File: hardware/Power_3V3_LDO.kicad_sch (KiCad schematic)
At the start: 5 parts, among them U1 MCP1826S

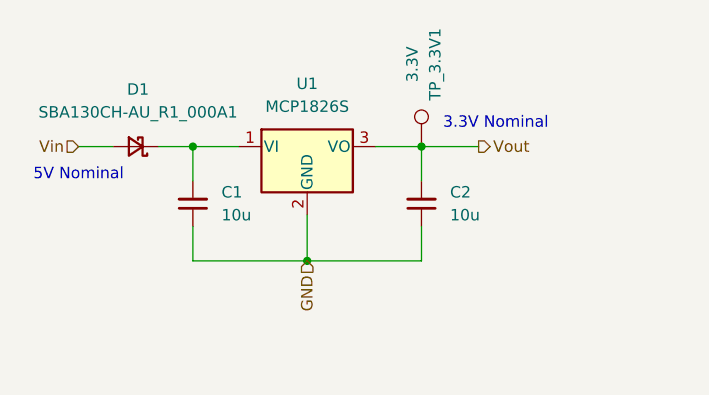
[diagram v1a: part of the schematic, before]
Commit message: finished schematic except for 12v buck boost
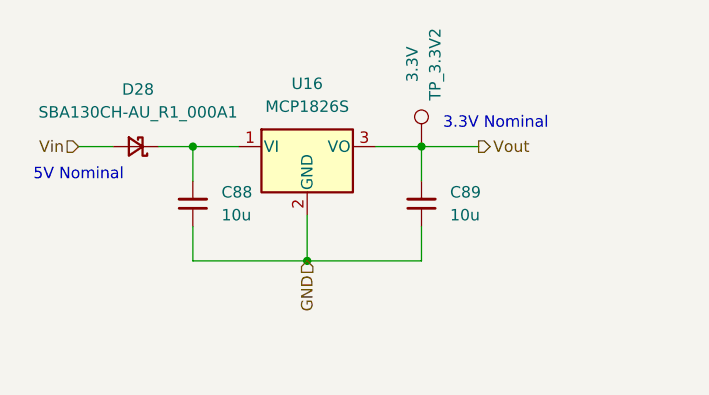
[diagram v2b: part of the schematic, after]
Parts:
- renumbered C1 to C88, C2 to C89, D1 to D28, TP_3.3V1 to TP_3.3V2, U1 to U16
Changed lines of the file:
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@@
 		(dnp no)
 		(fields_autoplaced yes)
-		(property "Reference" "C1"
+		(property "Reference" "C88"
 			(at 142.875 68.5735 0)
 			(show_name no)
@@
 			(project "PS-BPSLeader"
 				(path "/d4a4ed4f-0983-4aef-b212-0e3284ab3963/69244dac-f10b-499c-a2b2-3cdf1370aa1f/3ac4b541-f87d-4cd8-af8e-016705365d4a"
-					(reference "C1")
+					(reference "C88")
 					(unit 1)
 				)
@@
 		(dnp no)
 		(fields_autoplaced yes)
-		(property "Reference" "U1"
+		(property "Reference" "U16"
 			(at 152.4 56.515 0)
 			(show_name no)
@@
 			(project "PS-BPSLeader"
 				(path "/d4a4ed4f-0983-4aef-b212-0e3284ab3963/69244dac-f10b-499c-a2b2-3cdf1370aa1f/3ac4b541-f87d-4cd8-af8e-016705365d4a"
-					(reference "U1")
+					(reference "U16")
 					(unit 1)
 				)
@@
 		(dnp no)
 		(fields_autoplaced yes)
-		(property "Reference" "C2"
+		(property "Reference" "C89"
 			(at 168.275 68.5735 0)
 			(show_name no)
@@
 			(project "PS-BPSLeader"
 				(path "/d4a4ed4f-0983-4aef-b212-0e3284ab3963/69244dac-f10b-499c-a2b2-3cdf1370aa1f/3ac4b541-f87d-4cd8-af8e-016705365d4a"
-					(reference "C2")
+					(reference "C89")
 					(unit 1)
 				)
@@
 		(dnp no)
 		(fields_autoplaced yes)
-		(property "Reference" "D1"
+		(property "Reference" "D28"
 			(at 133.604 57.15 0)
 			(show_name no)
@@
 			(project "PS-BPSLeader"
 				(path "/d4a4ed4f-0983-4aef-b212-0e3284ab3963/69244dac-f10b-499c-a2b2-3cdf1370aa1f/3ac4b541-f87d-4cd8-af8e-016705365d4a"
-					(reference "D1")
+					(reference "D28")
 					(unit 1)
 				)
@@
 		(in_pos_files yes)
 		(dnp no)
-		(property "Reference" "TP_3.3V1"
+		(property "Reference" "TP_3.3V2"
 			(at 166.624 54.356 90)
 			(show_name no)
@@
 			(project "PS-BPSLeader"
 				(path "/d4a4ed4f-0983-4aef-b212-0e3284ab3963/69244dac-f10b-499c-a2b2-3cdf1370aa1f/3ac4b541-f87d-4cd8-af8e-016705365d4a"
-					(reference "TP_3.3V1")
-					(unit 1)
-				)
+					(reference "TP_3.3V2")
+					(unit 1)
+				)

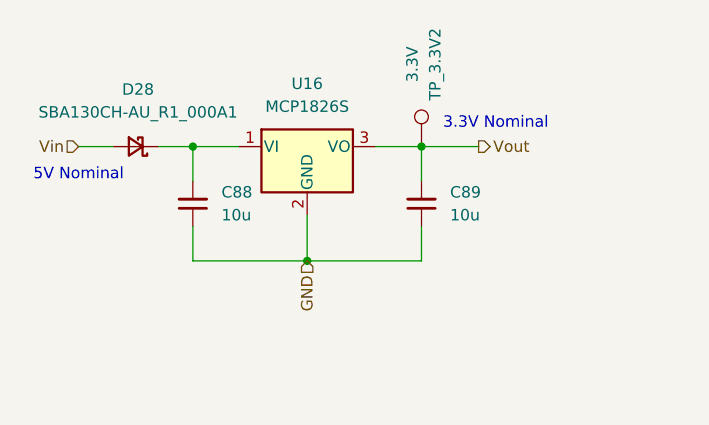
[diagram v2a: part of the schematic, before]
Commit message: added 12V buck boost
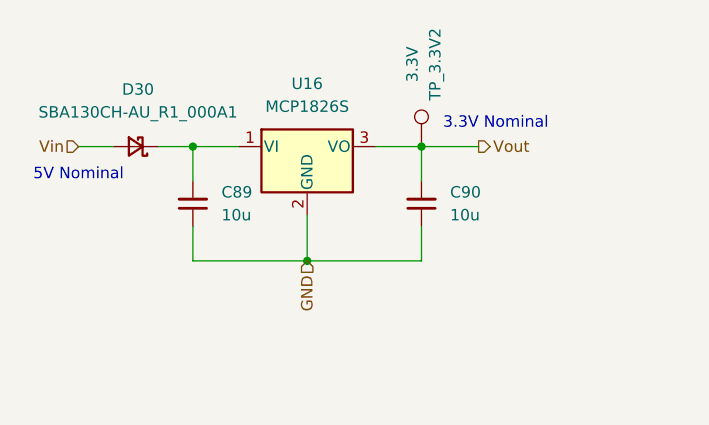
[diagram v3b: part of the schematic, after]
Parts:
- renumbered C88 to C89, C89 to C90, D28 to D30
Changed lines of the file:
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@@
 		(dnp no)
 		(fields_autoplaced yes)
-		(property "Reference" "C88"
+		(property "Reference" "C89"
 			(at 142.875 68.5735 0)
 			(show_name no)
@@
 			(project "PS-BPSLeader"
 				(path "/d4a4ed4f-0983-4aef-b212-0e3284ab3963/69244dac-f10b-499c-a2b2-3cdf1370aa1f/3ac4b541-f87d-4cd8-af8e-016705365d4a"
-					(reference "C88")
+					(reference "C89")
 					(unit 1)
 				)
@@
 		(dnp no)
 		(fields_autoplaced yes)
-		(property "Reference" "C89"
+		(property "Reference" "C90"
 			(at 168.275 68.5735 0)
 			(show_name no)
@@
 			(project "PS-BPSLeader"
 				(path "/d4a4ed4f-0983-4aef-b212-0e3284ab3963/69244dac-f10b-499c-a2b2-3cdf1370aa1f/3ac4b541-f87d-4cd8-af8e-016705365d4a"
-					(reference "C89")
+					(reference "C90")
 					(unit 1)
 				)
@@
 		(dnp no)
 		(fields_autoplaced yes)
-		(property "Reference" "D28"
+		(property "Reference" "D30"
 			(at 133.604 57.15 0)
 			(show_name no)
@@
 			(project "PS-BPSLeader"
 				(path "/d4a4ed4f-0983-4aef-b212-0e3284ab3963/69244dac-f10b-499c-a2b2-3cdf1370aa1f/3ac4b541-f87d-4cd8-af8e-016705365d4a"
-					(reference "D28")
-					(unit 1)
-				)
+					(reference "D30")
+					(unit 1)
+				)

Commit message: push gerbers and stuff
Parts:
- TP_3.3V2: now not fitted
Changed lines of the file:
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@@
 		(on_board yes)
 		(in_pos_files yes)
-		(dnp no)
+		(dnp yes)
 		(property "Reference" "TP_3.3V2"
 			(at 166.624 54.356 90)
